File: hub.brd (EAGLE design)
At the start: 64.1 x 51.7 mm, 51 parts, among them U1 LM3526, X1 12MHz

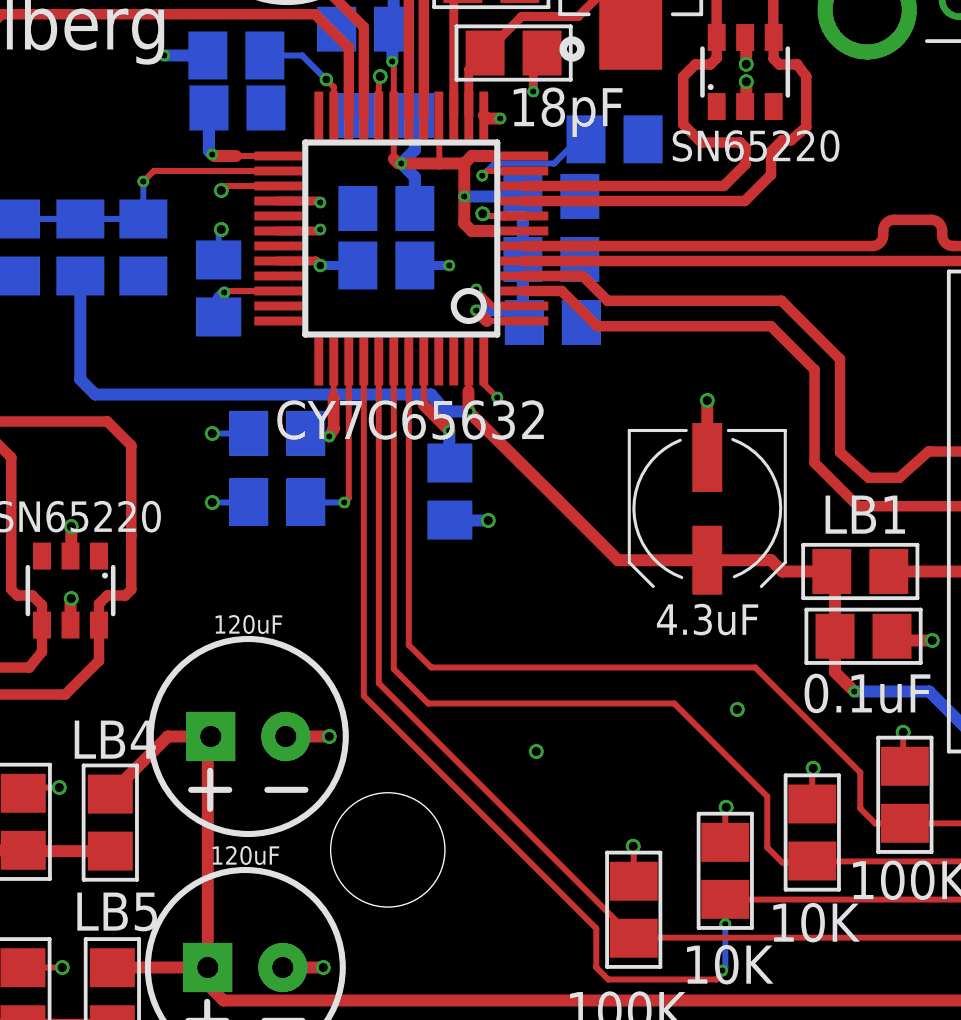
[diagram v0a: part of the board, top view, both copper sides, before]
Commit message: add and connect I2C EEPROM
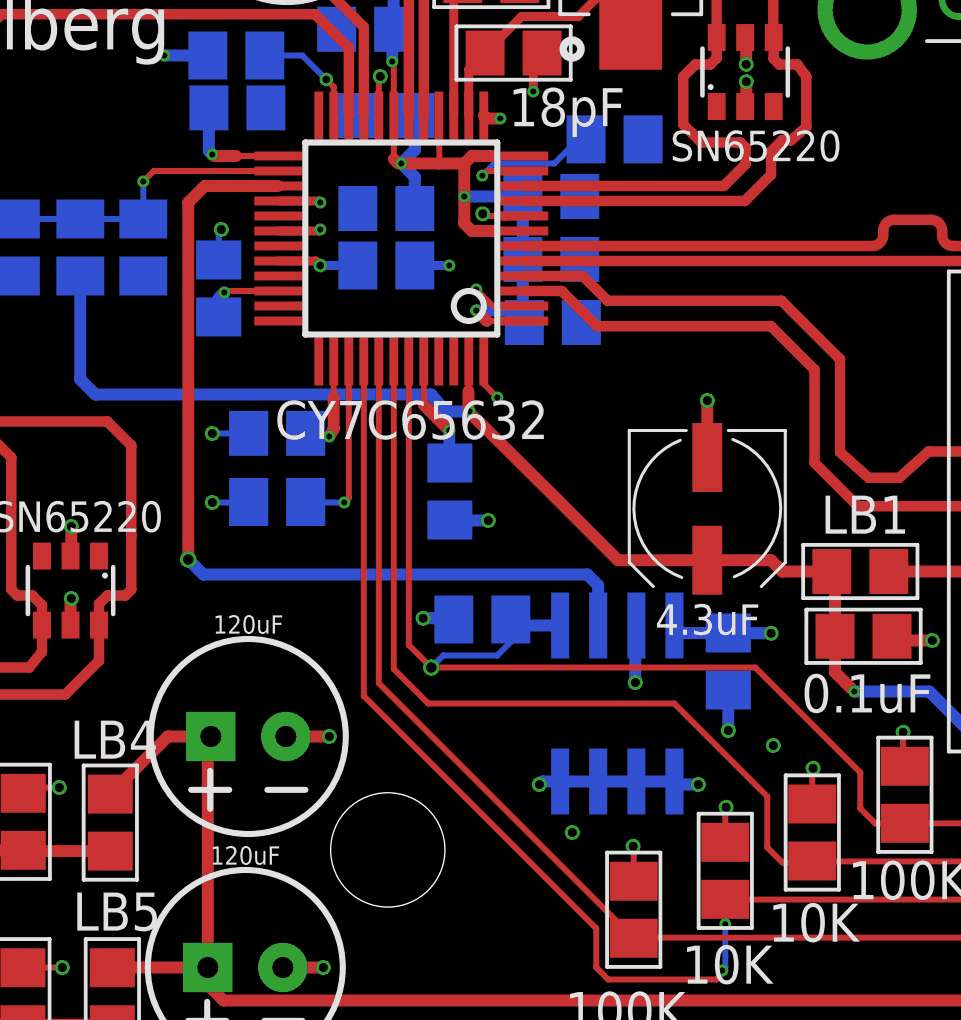
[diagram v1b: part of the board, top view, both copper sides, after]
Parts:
- added C6: 0.1uF, rcl:C0805
- added IC2: 24C02CSN, microchip:SO-08
- added R4: 10K, rcl:M0805
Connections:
- new net TEST_SCL: IC2.6, U$1.27
- net +3V3: now also C6.1, IC2.8, R4.1
- net GND: now also C6.2, IC2.1, IC2.2, IC2.3, IC2.4, IC2.7; no longer U$1.27
- net NENP1: now also IC2.5, R4.2
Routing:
- net TEST_SCL: track 0.00 -> 30.5 mm, vias 0 -> 1
- net GND: track 45.2 -> 51.9 mm, vias 121 -> 124
- net NENP1: track 33.0 -> 38.4 mm, vias 0 -> 1
- net +3V3: track 29.9 -> 33.4 mm, vias 14 -> 16
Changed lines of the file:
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@@
 <attribute name="VALUE" x="23.97" y="33.46" size="1.27" layer="26" rot="MR0"/>
+</element>
+<element name="IC2" library="microchip" library_urn="urn:adsk.eagle:library:294" package="SO-08" package3d_urn="urn:adsk.eagle:package:20804/2" value="24C02CSN" x="39.4" y="12.5" rot="MR0">
+<attribute name="DIGIKEY" value="24C02C/SN-ND" x="39.4" y="12.5" size="1.778" layer="28" rot="MR0" display="off"/>
+<attribute name="MF" value="MICROCHIP" x="39.4" y="12.5" size="1.778" layer="28" rot="MR0" display="off"/>
+<attribute name="MPN" value="24C02C/SN" x="39.4" y="12.5" size="1.778" layer="28" rot="MR0" display="off"/>
+<attribute name="OC_FARNELL" value="1607552" x="39.4" y="12.5" size="1.778" layer="28" rot="MR0" display="off"/>
+<attribute name="OC_NEWARK" value="96K4065" x="39.4" y="12.5" size="1.778" layer="28" rot="MR0" display="off"/>
+</element>
+<element name="R4" library="rcl" package="M0805" package3d_urn="urn:adsk.eagle:package:23556/1" value="10K" x="34.9" y="15.3" smashed="yes" rot="MR180">
+<attribute name="DIGIKEY" value="311-10.0KCRCT-ND" x="34.9" y="15.3" size="1.778" layer="28" rot="MR180" display="off"/>
+<attribute name="MPN" value="RC0805FR-0710KL" x="34.9" y="15.3" size="1.778" layer="28" rot="MR180" display="off"/>
+<attribute name="OC_MOUSER" value="603-RC0805FR-0710KL" x="34.9" y="15.3" size="1.778" layer="28" rot="MR180" display="off"/>
+<attribute name="VALUE" x="33.63" y="17.84" size="1.27" layer="28" rot="MR180"/>
+</element>
+<element name="C6" library="rcl" package="C0805" package3d_urn="urn:adsk.eagle:package:23617/2" value="0.1uF" x="43.1" y="13.9" rot="MR270">
+<attribute name="DIGIKEY" value="490-1666-1-ND" x="43.1" y="13.9" size="1.778" layer="28" rot="MR270" display="off"/>
+<attribute name="MPN" value="GRM21BR71H104KA01L" x="43.1" y="13.9" size="1.778" layer="28" rot="MR270" display="off"/>
+<attribute name="OC_MOUSER" value="81-GRM40X104K50L" x="43.1" y="13.9" size="1.778" layer="28" rot="MR270" display="off"/>
 </element>
 </elements>
@@
 </polygon>
 <contactref element="U$1" pad="37"/>
-<contactref element="U$1" pad="27"/>
 <contactref element="TSUP4" pad="5"/>
 <contactref element="TSUP4" pad="2"/>
@@
 <wire x1="9.8" y1="18.96" x2="9.8" y2="18.1" width="0.2" layer="1"/>
 <via x="26.2" y="28.3" extent="1-16" drill="0.3"/>
-<via x="26.2" y="29.6" extent="1-16" drill="0.3"/>
-<wire x1="28.1" y1="29.75" x2="26.35" y2="29.75" width="0.2" layer="1"/>
-<wire x1="26.35" y1="29.75" x2="26.2" y2="29.6" width="0.2" layer="1"/>
 <wire x1="26.114" y1="27.286" x2="26.114" y2="28.214" width="0.2" layer="16"/>
 <wire x1="26.114" y1="28.214" x2="26.2" y2="28.3" width="0.2" layer="16"/>
@@
 <wire x1="54.3" y1="30.2" x2="54.3" y2="31.05" width="0.4" layer="1"/>
 <via x="34.916" y="28.823" extent="1-16" drill="0.3"/>
-<via x="36.7" y="10.9" extent="1-16" drill="0.3"/>
-<via x="43.4" y="12.3" extent="1-16" drill="0.3"/>
+<via x="37.9" y="8.2" extent="1-16" drill="0.3"/>
+<via x="44.6" y="11.1" extent="1-16" drill="0.3"/>
 <wire x1="55.7" y1="23" x2="52.3" y2="23" width="0.4" layer="1"/>
 <wire x1="52.3" y1="23" x2="52.2" y2="22.9" width="0.4" layer="1"/>
@@
 <wire x1="35.4" y1="28.75" x2="35.63326875" y2="28.75" width="0.3" layer="1"/>
 <wire x1="36.3" y1="28.75" x2="35.63326875" y2="28.75" width="0.3" layer="1"/>
+<contactref element="IC2" pad="4"/>
+<contactref element="IC2" pad="1"/>
+<contactref element="IC2" pad="2"/>
+<contactref element="IC2" pad="3"/>
+<contactref element="IC2" pad="7"/>
+<contactref element="C6" pad="2"/>
+<via x="43.1" y="11.6" extent="1-16" drill="0.3"/>
+<wire x1="43.1" y1="11.6" x2="43.1" y2="12.95" width="0.4" layer="16"/>
+<via x="36.8" y="9.8" extent="1-16" drill="0.3"/>
+<via x="40" y="13.2" extent="1-16" drill="0.3"/>
+<via x="42.1" y="9.8" extent="1-16" drill="0.3"/>
+<wire x1="42.1" y1="9.8" x2="41.405" y2="9.8" width="0.4" layer="16"/>
+<wire x1="41.405" y1="9.8" x2="41.305" y2="9.9" width="0.4" layer="16"/>
+<wire x1="41.305" y1="9.9" x2="40.035" y2="9.9" width="0.4" layer="16"/>
+<wire x1="40.035" y1="9.9" x2="38.765" y2="9.9" width="0.4" layer="16"/>
+<wire x1="38.765" y1="9.9" x2="37.495" y2="9.9" width="0.4" layer="16"/>
+<wire x1="37.495" y1="9.9" x2="36.9" y2="9.9" width="0.4" layer="16"/>
+<wire x1="36.9" y1="9.9" x2="36.8" y2="9.8" width="0.4" layer="16"/>
+<wire x1="40" y1="13.2" x2="40" y2="15.065" width="0.4" layer="16"/>
+<wire x1="40" y1="15.065" x2="40.035" y2="15.1" width="0.4" layer="16"/>
 </signal>
 <signal name="D0_N" class="1">
@@
 <wire x1="29.95" y1="21.65" x2="29.8" y2="21.4" width="0.4" layer="1"/>
 <via x="29.8" y="21.4" extent="1-16" drill="0.2"/>
-<wire x1="29.8" y1="21.4" x2="29.018" y2="21.5" width="0.2" layer="16"/>
+<wire x1="29.8" y1="21.4" x2="29.018" y2="21.5" width="0" layer="19" extent="1-16"/>
 <wire x1="29.018" y1="21.5" x2="29.014" y2="21.504" width="0.2" layer="16"/>
 <via x="39.929" y="7.741" extent="1-16" drill="0.3"/>
@@
 <wire x1="28.1" y1="28.25" x2="29.45" y2="28.25" width="0.3" layer="1"/>
 <wire x1="29.45" y1="28.25" x2="29.5" y2="28.3" width="0.3" layer="1"/>
+<contactref element="R4" pad="1"/>
+<contactref element="C6" pad="1"/>
+<contactref element="IC2" pad="8"/>
+<wire x1="41.305" y1="15.1" x2="41.555" y2="14.85" width="0.4" layer="16"/>
+<wire x1="43.1" y1="14.85" x2="41.555" y2="14.85" width="0.4" layer="16"/>
+<via x="44.529" y="14.841" extent="1-16" drill="0.3"/>
+<wire x1="44.529" y1="14.841" x2="43.109" y2="14.841" width="0.4" layer="16"/>
+<wire x1="43.109" y1="14.841" x2="43.1" y2="14.85" width="0.4" layer="16"/>
+<via x="32.929" y="15.341" extent="1-16" drill="0.3"/>
+<wire x1="32.929" y1="15.341" x2="33.909" y2="15.341" width="0.4" layer="16"/>
+<wire x1="33.909" y1="15.341" x2="33.95" y2="15.3" width="0.4" layer="16"/>
 </signal>
 <signal name="NENP1">
@@
 <wire x1="47.5" y1="10.2" x2="44" y2="13.7" width="0.2" layer="1"/>
 <wire x1="44" y1="13.7" x2="33.2" y2="13.7" width="0.2" layer="1"/>
+<contactref element="IC2" pad="5"/>
+<contactref element="R4" pad="2"/>
+<wire x1="35.975" y1="15.175" x2="35.85" y2="15.3" width="0.4" layer="16"/>
+<wire x1="35.975" y1="15.175" x2="36.05" y2="15.1" width="0.4" layer="16"/>
+<wire x1="36.05" y1="15.1" x2="37.495" y2="15.1" width="0.4" layer="16"/>
+<via x="33.2" y="13.7" extent="1-16" drill="0.35"/>
+<wire x1="33.2" y1="13.7" x2="33.6" y2="14.1" width="0.2" layer="16"/>
+<wire x1="33.6" y1="14.1" x2="35.4" y2="14.1" width="0.2" layer="16"/>
+<wire x1="35.4" y1="14.1" x2="35.975" y2="14.675" width="0.2" layer="16"/>
+<wire x1="35.975" y1="14.675" x2="35.975" y2="15.175" width="0.2" layer="16"/>
 </signal>
 <signal name="NENP2">
@@
 <wire x1="29.5" y1="27.1" x2="30.75" y2="27.1" width="0.3" layer="16"/>
 </signal>
+<signal name="TEST_SCL">
+<contactref element="U$1" pad="27"/>
+<contactref element="IC2" pad="6"/>
+<wire x1="38.765" y1="15.1" x2="38.765" y2="16.435" width="0.4" layer="16"/>
+<wire x1="38.765" y1="16.435" x2="38.4" y2="16.8" width="0.4" layer="16"/>
+<wire x1="38.4" y1="16.8" x2="25.6" y2="16.8" width="0.4" layer="16"/>
+<wire x1="25.6" y1="16.8" x2="25.1" y2="17.3" width="0.4" layer="16"/>
+<via x="25.1" y="17.3" extent="1-16" drill="0.35"/>
+<wire x1="25.1" y1="17.3" x2="25.1" y2="29.2" width="0.4" layer="1"/>
+<wire x1="25.65" y1="29.75" x2="28.1" y2="29.75" width="0.4" layer="1"/>
+<wire x1="25.1" y1="29.2" x2="25.65" y2="29.75" width="0.4" layer="1"/>
+</signal>
 </signals>

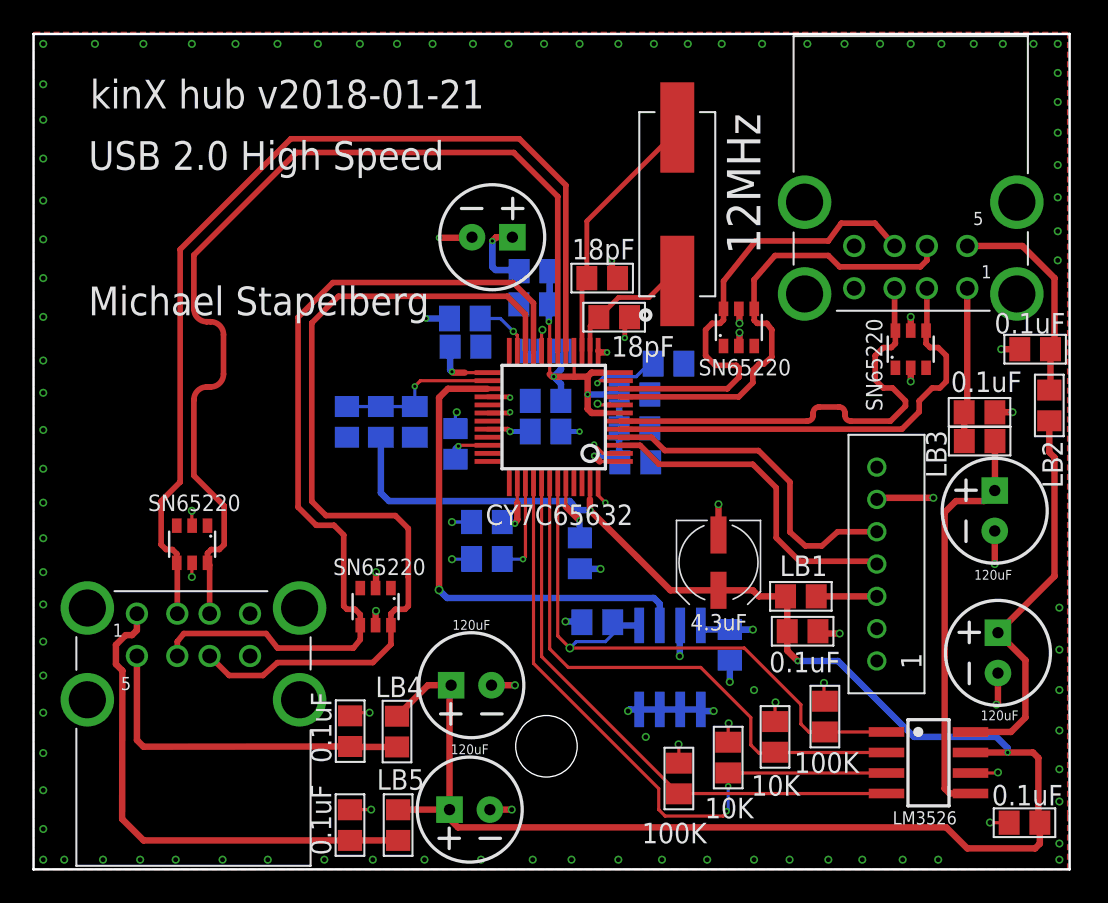
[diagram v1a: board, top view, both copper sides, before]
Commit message: enlarge drill holes for DRC
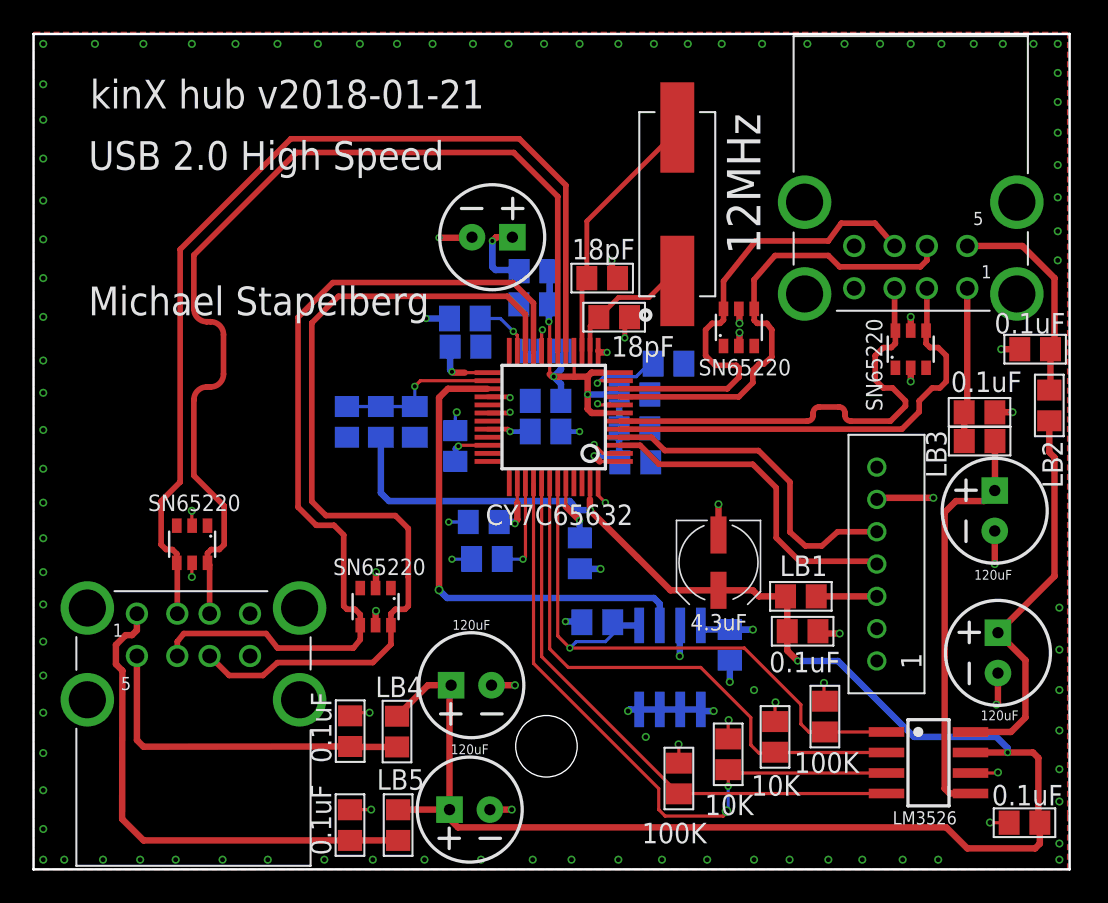
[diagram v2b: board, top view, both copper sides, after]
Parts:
- moved R24 0.20 mm to (43.0, 7.12)
- moved C12 0.20 mm to (27.9, 21.5)
- moved C10 0.13 mm to (26.1, 26.2)
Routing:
- net +3V3: track 33.4 -> 34.6 mm

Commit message: move vias for DRC
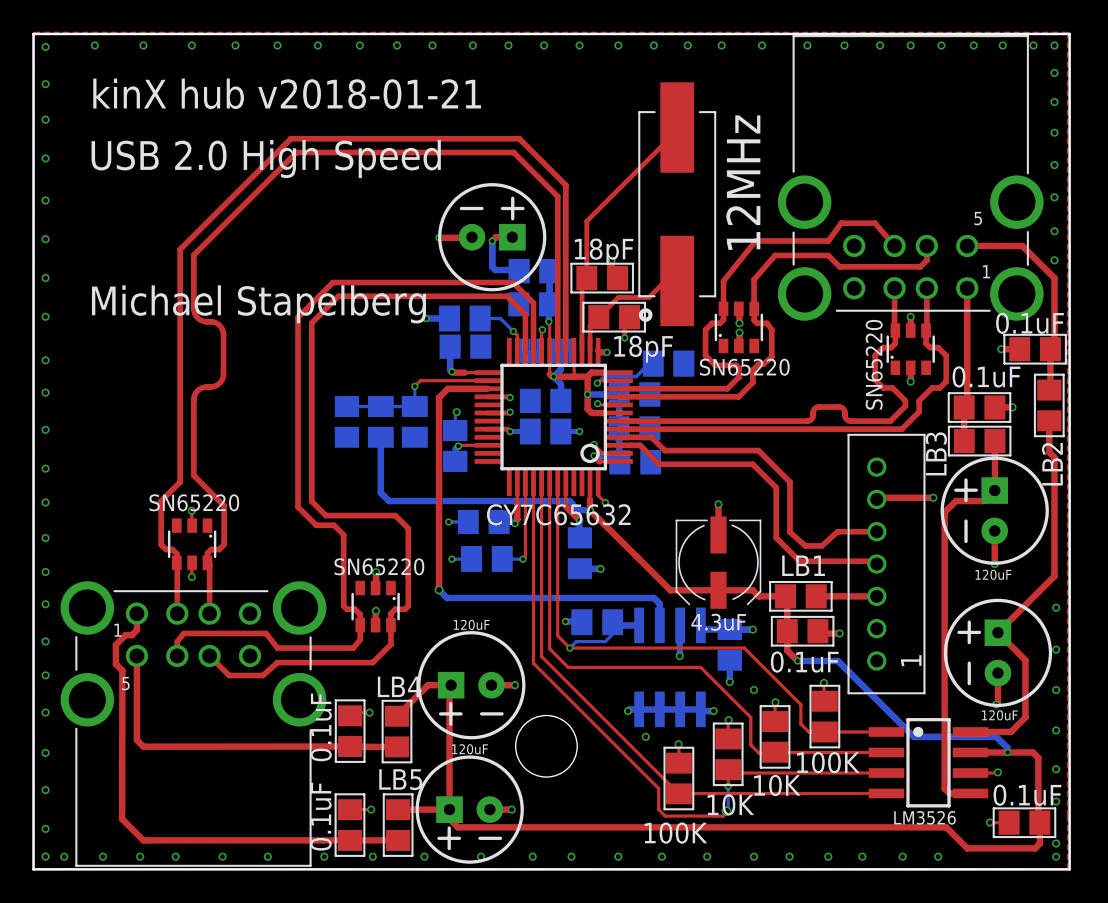
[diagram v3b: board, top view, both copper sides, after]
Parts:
- moved C20 0.30 mm to (58.6, 28.6)
